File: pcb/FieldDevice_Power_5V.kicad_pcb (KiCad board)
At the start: 2 copper layers, 51.6 x 48 mm, 160 parts, among them J1 Itp_1, J2 V in 6-18V, J3 Itp_2, J4 V out 5V, J5 Vtp_2, J6 Vtp_1, J7 Battery, U1 TPS54232

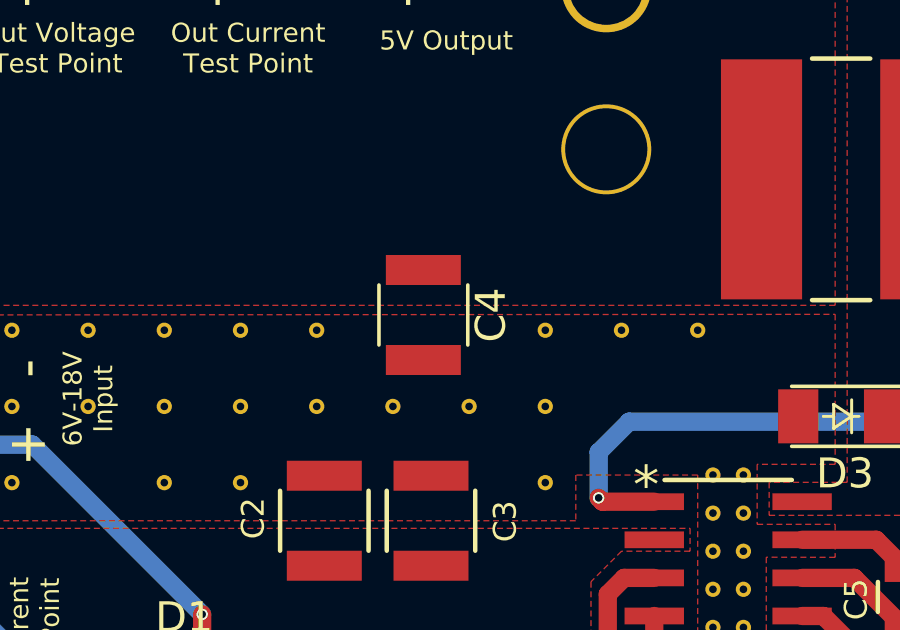
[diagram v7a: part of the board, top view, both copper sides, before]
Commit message: Changed the footprint for C4
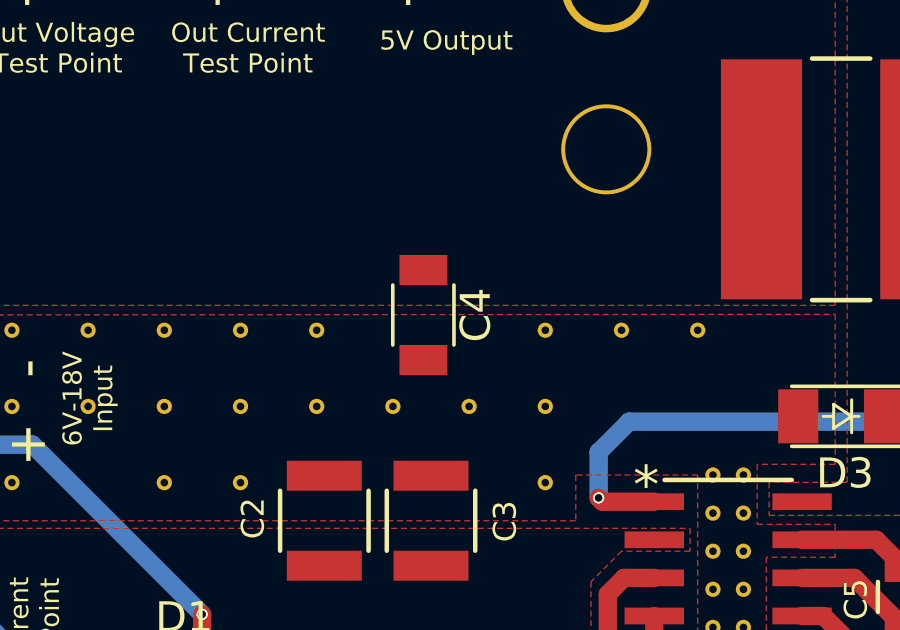
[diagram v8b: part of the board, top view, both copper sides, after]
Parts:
- C4: footprint Capacitors_SMD:C_1210 -> Capacitors_SMD:C_1206
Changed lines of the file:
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@@
 (kicad_pcb (version 4) (host pcbnew 4.0.7)
   (general
-    (links 176)
+    (links 174)
     (no_connects 0)
     (area 63.932999 44.120999 115.645001 92.277001)
@@
     (add_net "Net-(D1-Pad2)")
   )
-  (module Capacitors_SMD:C_1210 (layer F.Cu)
-    (at 84.074 61.722 270)
-    (descr "Capacitor SMD 1210, reflow soldering, AVX (see smccp.pdf)")
-    (tags "capacitor 1210")
-    (attr smd)
-    (fp_text reference C4 (at 0 -2.25 270) (layer F.SilkS)
-      (effects (font (size 1 1) (thickness 0.15)))
-    )
-    (fp_text value "47.0 μF" (at 0 2.5 270) (layer F.Fab)
-      (effects (font (size 1 1) (thickness 0.15)))
-    )
-    (fp_text user %R (at 0 -2.25 270) (layer F.Fab)
-      (effects (font (size 1 1) (thickness 0.15)))
-    )
-    (fp_line (start -1.6 1.25) (end -1.6 -1.25) (layer F.Fab) (width 0.1))
-    (fp_line (start 1.6 1.25) (end -1.6 1.25) (layer F.Fab) (width 0.1))
-    (fp_line (start 1.6 -1.25) (end 1.6 1.25) (layer F.Fab) (width 0.1))
-    (fp_line (start -1.6 -1.25) (end 1.6 -1.25) (layer F.Fab) (width 0.1))
-    (fp_line (start 1 -1.48) (end -1 -1.48) (layer F.SilkS) (width 0.12))
-    (fp_line (start -1 1.48) (end 1 1.48) (layer F.SilkS) (width 0.12))
-    (fp_line (start -2.25 -1.5) (end 2.25 -1.5) (layer F.CrtYd) (width 0.05))
-    (fp_line (start -2.25 -1.5) (end -2.25 1.5) (layer F.CrtYd) (width 0.05))
-    (fp_line (start 2.25 1.5) (end 2.25 -1.5) (layer F.CrtYd) (width 0.05))
-    (fp_line (start 2.25 1.5) (end -2.25 1.5) (layer F.CrtYd) (width 0.05))
-    (pad 1 smd rect (at -1.5 0 270) (size 1 2.5) (layers F.Cu F.Paste F.Mask)
-      (net 6 /Vout))
-    (pad 2 smd rect (at 1.5 0 270) (size 1 2.5) (layers F.Cu F.Paste F.Mask)
-      (net 1 GND))
-    (model Capacitors_SMD.3dshapes/C_1210.wrl
-      (at (xyz 0 0 0))
-      (scale (xyz 1 1 1))
-      (rotate (xyz 0 0 0))
-    )
-  )
   (module FieldDevice_Power_5V:STITCH_VIA (layer F.Cu)
     (at 72.9 86.1)
@@
       (at (xyz 0 0 0))
       (scale (xyz 1 1 1))
+      (rotate (xyz 0 0 0))
+    )
+  )
+  (module Capacitors_SMD:C_1206 (layer F.Cu)
+    (at 84.074 61.722 270)
+    (descr "Capacitor SMD 1206, reflow soldering, AVX (see smccp.pdf)")
+    (tags "capacitor 1206")
+    (attr smd)
+    (fp_text reference C4 (at 0 -1.75 270) (layer F.SilkS)
+      (effects (font (size 1 1) (thickness 0.15)))
+    )
+    (fp_text value "47.0 μF" (at 0 2 270) (layer F.Fab)
+      (effects (font (size 1 1) (thickness 0.15)))
+    )
+    (fp_text user %R (at 0 -1.75 270) (layer F.Fab)
+      (effects (font (size 1 1) (thickness 0.15)))
+    )
+    (fp_line (start -1.6 0.8) (end -1.6 -0.8) (layer F.Fab) (width 0.1))
+    (fp_line (start 1.6 0.8) (end -1.6 0.8) (layer F.Fab) (width 0.1))
+    (fp_line (start 1.6 -0.8) (end 1.6 0.8) (layer F.Fab) (width 0.1))
+    (fp_line (start -1.6 -0.8) (end 1.6 -0.8) (layer F.Fab) (width 0.1))
+    (fp_line (start 1 -1.02) (end -1 -1.02) (layer F.SilkS) (width 0.12))
+    (fp_line (start -1 1.02) (end 1 1.02) (layer F.SilkS) (width 0.12))
+    (fp_line (start -2.25 -1.05) (end 2.25 -1.05) (layer F.CrtYd) (width 0.05))
+    (fp_line (start -2.25 -1.05) (end -2.25 1.05) (layer F.CrtYd) (width 0.05))
+    (fp_line (start 2.25 1.05) (end 2.25 -1.05) (layer F.CrtYd) (width 0.05))
+    (fp_line (start 2.25 1.05) (end -2.25 1.05) (layer F.CrtYd) (width 0.05))
+    (pad 1 smd rect (at -1.5 0 270) (size 1 1.6) (layers F.Cu F.Paste F.Mask)
+      (net 6 /Vout))
+    (pad 2 smd rect (at 1.5 0 270) (size 1 1.6) (layers F.Cu F.Paste F.Mask)
+      (net 1 GND))
+    (model Capacitors_SMD.3dshapes/C_1206.wrl
+      (at (xyz 0 0 0))
+      (scale (xyz 1 1 1))
